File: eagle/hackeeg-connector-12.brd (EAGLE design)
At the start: 77.7 x 27.9 mm, 13 parts

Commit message: replaced OSTTA120161B with OSTTA120161 library
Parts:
- WIRE-CONNECTOR: value OSTTA120161B -> OSTTA120161; device OSTTA120161B:ONSHORE_OSTTA120161B -> OSTTA120161:ONSHORE_OSTTA120161
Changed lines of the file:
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@@
 <attribute name="VALUE" x="85.979" y="24.511" size="0.6096" layer="27" font="vector" ratio="20" align="top-center"/>
 </element>
-<element name="WIRE-CONNECTOR" library="OSTTA120161B" package="ONSHORE_OSTTA120161B" value="OSTTA120161B" x="83.82" y="8.89" smashed="yes" rot="MR0">
+<element name="WIRE-CONNECTOR" library="OSTTA120161" package="ONSHORE_OSTTA120161" value="OSTTA120161" x="83.82" y="8.89" smashed="yes" rot="MR0">
 <attribute name="AVAILABILITY" value="Unavailable" x="83.82" y="8.89" size="1.778" layer="28" rot="MR0" display="off"/>
 <attribute name="DESCRIPTION" value=" TERM BLK 12P SIDE ENTRY 5MM PCB " x="83.82" y="8.89" size="1.778" layer="28" rot="MR0" display="off"/>

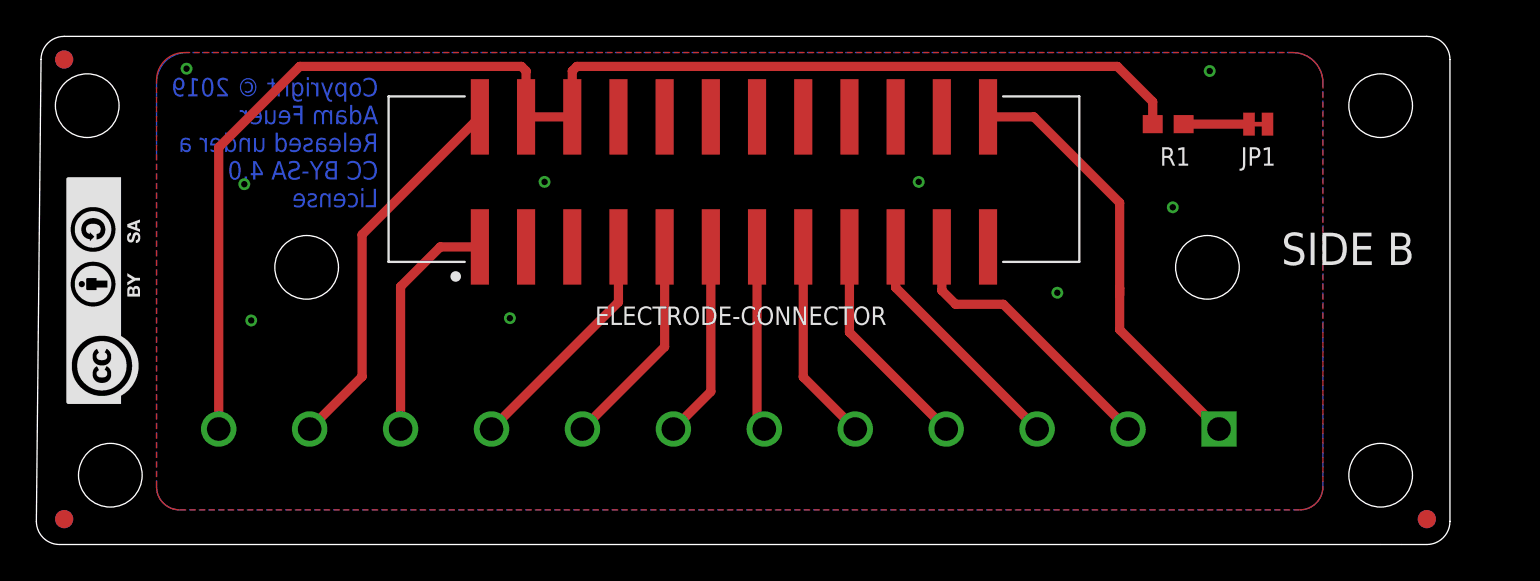
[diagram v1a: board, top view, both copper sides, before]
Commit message: add connector version numbers to schematic and PCB
- also added board names to PCBs
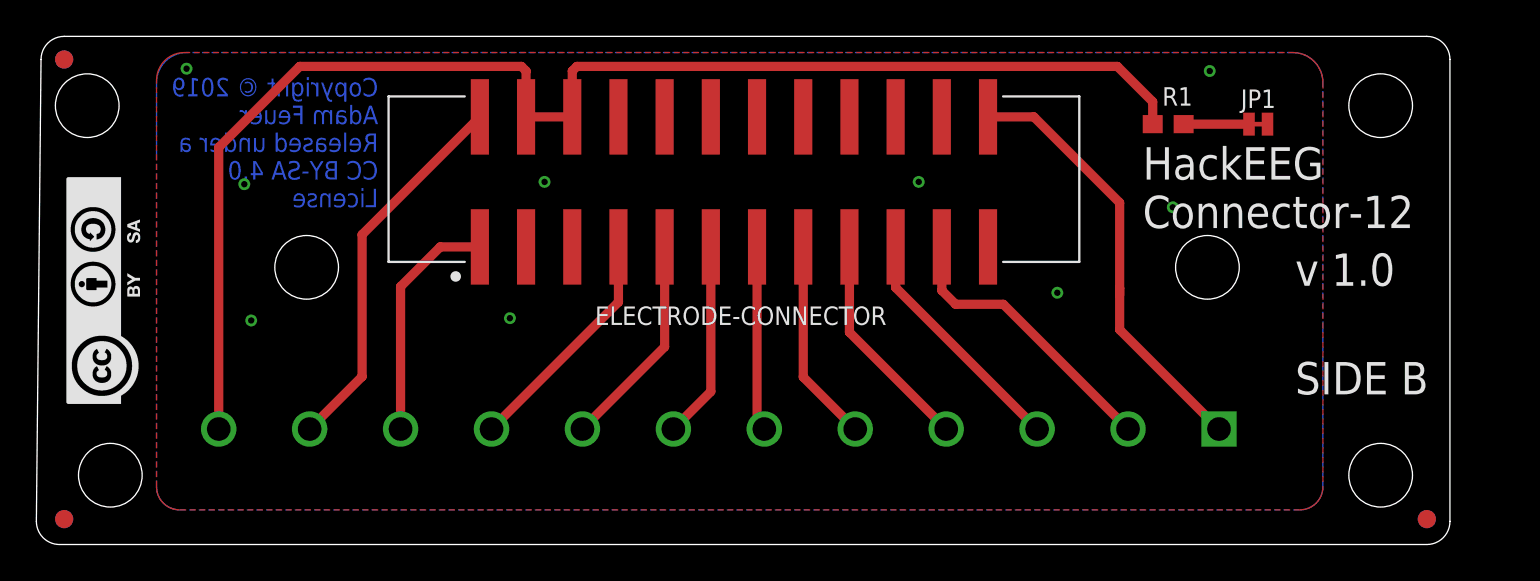
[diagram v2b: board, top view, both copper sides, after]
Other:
- outline, holes or cut-outs redrawn
- board text added: "HackEEG Connector-12"
- board text added: "v 1.0"
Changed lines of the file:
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@@
 <?xml version="1.0" encoding="utf-8"?>
 <!DOCTYPE eagle SYSTEM "eagle.dtd">
-<eagle version="9.1.2">
+<eagle version="9.4.0">
 <drawing>
 <settings>
@@
 <wire x1="19.05" y1="29.21" x2="18.793565625" y2="3.822978125" width="0" layer="20"/>
 <wire x1="18.793565625" y1="3.822978125" x2="20.0635" y2="2.54" width="0" layer="20" curve="90.578748"/>
-<wire x1="20.0635" y1="2.54" x2="92.71" y2="2.54" width="0" layer="20"/>
-<wire x1="92.71" y1="2.54" x2="93.846296875" y2="2.54" width="0" layer="20"/>
+<wire x1="20.0635" y1="2.54" x2="95.25" y2="2.54" width="0" layer="20"/>
 <wire x1="20.32" y1="30.48" x2="95.25" y2="30.48" width="0" layer="20"/>
 <wire x1="95.25" y1="30.48" x2="96.52" y2="29.21" width="0" layer="20" curve="-90"/>
 <wire x1="96.52" y1="29.21" x2="96.52" y2="3.81" width="0" layer="20"/>
 <wire x1="96.52" y1="3.81" x2="95.25" y2="2.54" width="0" layer="20" curve="-90"/>
-<wire x1="95.25" y1="2.54" x2="93.846296875" y2="2.54" width="0" layer="20"/>
 <wire x1="20.32" y1="30.48" x2="19.05" y2="29.21" width="0" layer="20" curve="90"/>
-<text x="94.615" y="20.32" size="1.778" layer="26" rot="MR0">SIDE A</text>
-<text x="87.249" y="17.907" size="1.778" layer="25">SIDE B</text>
+<text x="95.377" y="8.509" size="1.778" layer="26" rot="MR0">SIDE A</text>
+<text x="88.011" y="10.795" size="1.778" layer="25">SIDE B</text>
 <hole x="33.655" y="17.78" drill="3.49999375"/>
 <hole x="83.185" y="17.78" drill="3.49999375"/>
@@
 <text x="75.946" y="2.921" size="1.27" layer="26" rot="MR0">IN7P</text>
 <text x="80.772" y="2.921" size="1.27" layer="26" rot="MR0">IN8P</text>
+<text x="79.629" y="19.939" size="1.778" layer="25">HackEEG
+Connector-12</text>
+<text x="88.011" y="16.764" size="1.778" layer="25">v 1.0</text>
 </plain>
 <attributes>
@@
 <attribute name="VALUE" x="38.0449" y="14.83696875" size="1.78313125" layer="27"/>
 </element>
-<element name="FRAME1" library="SparkFun-Aesthetics" library_urn="urn:adsk.eagle:library:507" package="CREATIVE_COMMONS" package3d_urn="urn:adsk.eagle:package:37121/1" value="FRAME-LETTER" x="24.13" y="-10.16"/>
-<element name="U$1" library="endless-knot" package="ENDLESSKNOT-MEDIUM" value="ENDLESSKNOTENDLESSKNOT-MEDIUM" x="30.099" y="23.749" rot="MR0"/>
-<element name="U$13" library="creative-commons" package="CC-BY-SA" value="CC-BY-SA" x="24.765" y="10.16" rot="R90"/>
-<element name="FD1" library="SparkFun-Aesthetics" library_urn="urn:adsk.eagle:library:507" package="FIDUCIAL-1X2" package3d_urn="urn:adsk.eagle:package:37108/1" value="FIDUCIAL1X2" x="20.32" y="3.937"/>
-<element name="FD2" library="SparkFun-Aesthetics" library_urn="urn:adsk.eagle:library:507" package="FIDUCIAL-1X2" package3d_urn="urn:adsk.eagle:package:37108/1" value="FIDUCIAL1X2" x="20.32" y="29.21"/>
-<element name="FD3" library="SparkFun-Aesthetics" library_urn="urn:adsk.eagle:library:507" package="FIDUCIAL-1X2" package3d_urn="urn:adsk.eagle:package:37108/1" value="FIDUCIAL1X2" x="95.25" y="3.937"/>
-<element name="FD4" library="SparkFun-Aesthetics" library_urn="urn:adsk.eagle:library:507" package="FIDUCIAL-1X2" package3d_urn="urn:adsk.eagle:package:37108/1" value="FIDUCIAL1X2" x="95.25" y="3.937" rot="MR0"/>
-<element name="FD5" library="SparkFun-Aesthetics" library_urn="urn:adsk.eagle:library:507" package="FIDUCIAL-1X2" package3d_urn="urn:adsk.eagle:package:37108/1" value="FIDUCIAL1X2" x="20.32" y="29.21" rot="MR0"/>
-<element name="FD6" library="SparkFun-Aesthetics" library_urn="urn:adsk.eagle:library:507" package="FIDUCIAL-1X2" package3d_urn="urn:adsk.eagle:package:37108/1" value="FIDUCIAL1X2" x="20.32" y="3.937" rot="MR0"/>
+<element name="FRAME1" library="SparkFun-Aesthetics" library_urn="urn:adsk.eagle:library:507" package="CREATIVE_COMMONS" package3d_urn="urn:adsk.eagle:package:37121/1" value="FRAME-LETTER" x="24.13" y="-10.16" smashed="yes"/>
+<element name="U$1" library="endless-knot" package="ENDLESSKNOT-MEDIUM" value="ENDLESSKNOTENDLESSKNOT-MEDIUM" x="30.099" y="23.749" smashed="yes" rot="MR0"/>
+<element name="U$13" library="creative-commons" package="CC-BY-SA" value="CC-BY-SA" x="24.765" y="10.16" smashed="yes" rot="R90"/>
+<element name="FD1" library="SparkFun-Aesthetics" library_urn="urn:adsk.eagle:library:507" package="FIDUCIAL-1X2" package3d_urn="urn:adsk.eagle:package:37108/1" value="FIDUCIAL1X2" x="20.32" y="3.937" smashed="yes"/>
+<element name="FD2" library="SparkFun-Aesthetics" library_urn="urn:adsk.eagle:library:507" package="FIDUCIAL-1X2" package3d_urn="urn:adsk.eagle:package:37108/1" value="FIDUCIAL1X2" x="20.32" y="29.21" smashed="yes"/>
+<element name="FD3" library="SparkFun-Aesthetics" library_urn="urn:adsk.eagle:library:507" package="FIDUCIAL-1X2" package3d_urn="urn:adsk.eagle:package:37108/1" value="FIDUCIAL1X2" x="95.25" y="3.937" smashed="yes"/>
+<element name="FD4" library="SparkFun-Aesthetics" library_urn="urn:adsk.eagle:library:507" package="FIDUCIAL-1X2" package3d_urn="urn:adsk.eagle:package:37108/1" value="FIDUCIAL1X2" x="95.25" y="3.937" smashed="yes" rot="MR0"/>
+<element name="FD5" library="SparkFun-Aesthetics" library_urn="urn:adsk.eagle:library:507" package="FIDUCIAL-1X2" package3d_urn="urn:adsk.eagle:package:37108/1" value="FIDUCIAL1X2" x="20.32" y="29.21" smashed="yes" rot="MR0"/>
+<element name="FD6" library="SparkFun-Aesthetics" library_urn="urn:adsk.eagle:library:507" package="FIDUCIAL-1X2" package3d_urn="urn:adsk.eagle:package:37108/1" value="FIDUCIAL1X2" x="20.32" y="3.937" smashed="yes" rot="MR0"/>
 <element name="R1" library="SparkFun-Resistors" library_urn="urn:adsk.eagle:library:532" package="0603" package3d_urn="urn:adsk.eagle:package:39650/1" value="0" x="81.026" y="25.654" smashed="yes">
-<attribute name="NAME" x="81.407" y="23.368" size="1.016" layer="25" font="vector" ratio="20" align="bottom-center"/>
+<attribute name="NAME" x="81.534" y="26.67" size="1.016" layer="25" font="vector" ratio="20" align="bottom-center"/>
 <attribute name="PROD_ID" value="RES-08609" x="81.026" y="25.654" size="1.778" layer="27" display="off"/>
 <attribute name="VALUE" x="81.026" y="24.892" size="0.6096" layer="27" font="vector" ratio="20" align="top-center"/>
 </element>
 <element name="JP1" library="SparkFun-Jumpers" library_urn="urn:adsk.eagle:library:528" package="SMT-JUMPER_2_NC_TRACE_NO-SILK" package3d_urn="urn:adsk.eagle:package:39286/1" value="JUMPER-SMT_2_NC_TRACE_NO-SILK" x="85.979" y="25.654" smashed="yes">
-<attribute name="NAME" x="85.979" y="23.368" size="1.016" layer="25" font="vector" ratio="20" align="bottom-center"/>
+<attribute name="NAME" x="85.979" y="26.543" size="1.016" layer="25" font="vector" ratio="20" align="bottom-center"/>
 <attribute name="VALUE" x="85.979" y="24.511" size="0.6096" layer="27" font="vector" ratio="20" align="top-center"/>
 </element>

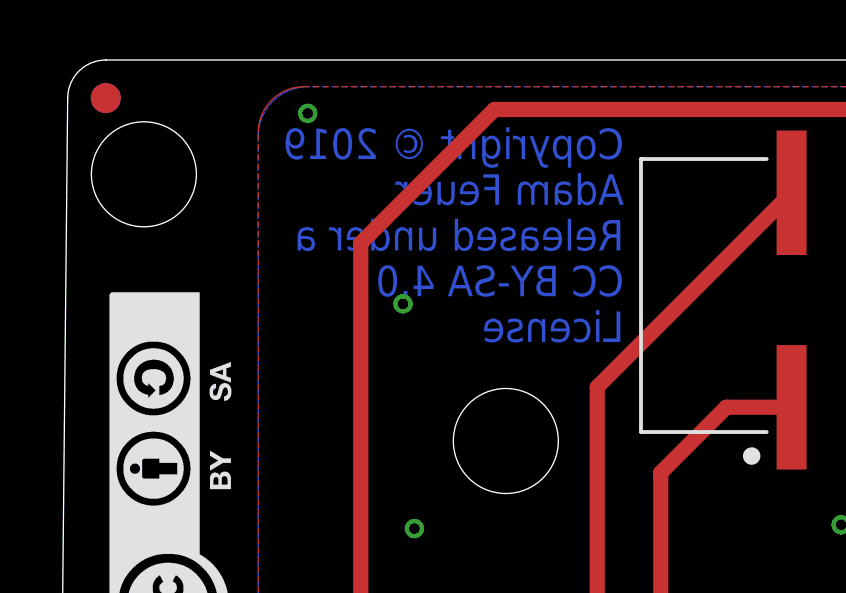
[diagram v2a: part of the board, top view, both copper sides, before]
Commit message: minor board legend updates
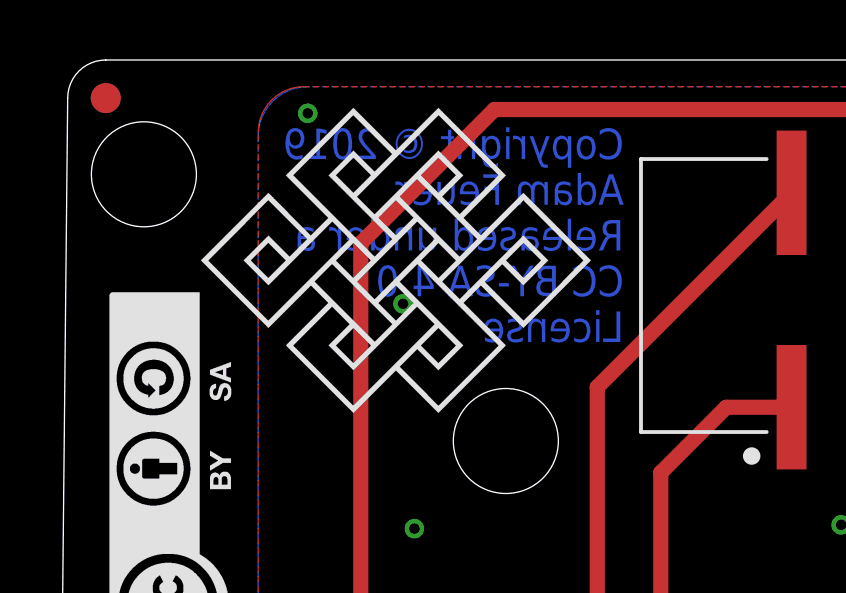
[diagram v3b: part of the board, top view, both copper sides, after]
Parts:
- flipped U$1 to the top
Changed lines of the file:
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@@
 <layer number="14" name="Route14" color="22" fill="1" visible="no" active="no"/>
 <layer number="15" name="Route15" color="23" fill="1" visible="no" active="no"/>
-<layer number="16" name="Bottom" color="1" fill="1" visible="no" active="yes"/>
+<layer number="16" name="Bottom" color="1" fill="1" visible="yes" active="yes"/>
 <layer number="17" name="Pads" color="2" fill="1" visible="yes" active="yes"/>
 <layer number="18" name="Vias" color="2" fill="1" visible="yes" active="yes"/>
@@
 <text x="60.452" y="2.921" size="1.27" layer="26" rot="MR0">IN4P</text>
 <text x="65.532" y="2.921" size="1.27" layer="26" rot="MR0">IN5P</text>
-<text x="70.485" y="2.794" size="1.27" layer="26" rot="MR0">IN6P</text>
+<text x="70.485" y="2.921" size="1.27" layer="26" rot="MR0">IN6P</text>
 <text x="75.946" y="2.921" size="1.27" layer="26" rot="MR0">IN7P</text>
 <text x="80.772" y="2.921" size="1.27" layer="26" rot="MR0">IN8P</text>
@@
 </element>
 <element name="FRAME1" library="SparkFun-Aesthetics" library_urn="urn:adsk.eagle:library:507" package="CREATIVE_COMMONS" package3d_urn="urn:adsk.eagle:package:37121/1" value="FRAME-LETTER" x="24.13" y="-10.16" smashed="yes"/>
-<element name="U$1" library="endless-knot" package="ENDLESSKNOT-MEDIUM" value="ENDLESSKNOTENDLESSKNOT-MEDIUM" x="30.099" y="23.749" smashed="yes" rot="MR0"/>
+<element name="U$1" library="endless-knot" package="ENDLESSKNOT-MEDIUM" value="ENDLESSKNOTENDLESSKNOT-MEDIUM" x="30.099" y="23.749" smashed="yes"/>
 <element name="U$13" library="creative-commons" package="CC-BY-SA" value="CC-BY-SA" x="24.765" y="10.16" smashed="yes" rot="R90"/>
 <element name="FD1" library="SparkFun-Aesthetics" library_urn="urn:adsk.eagle:library:507" package="FIDUCIAL-1X2" package3d_urn="urn:adsk.eagle:package:37108/1" value="FIDUCIAL1X2" x="20.32" y="3.937" smashed="yes"/>
